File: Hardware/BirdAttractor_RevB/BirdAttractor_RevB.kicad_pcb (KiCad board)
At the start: 2 copper layers, 48.3 x 48.3 mm, 15 parts, among them P1 CONN_01X06, U1 PR_Relay_V23079, U2 DS1305, Y1 Crystal_Small

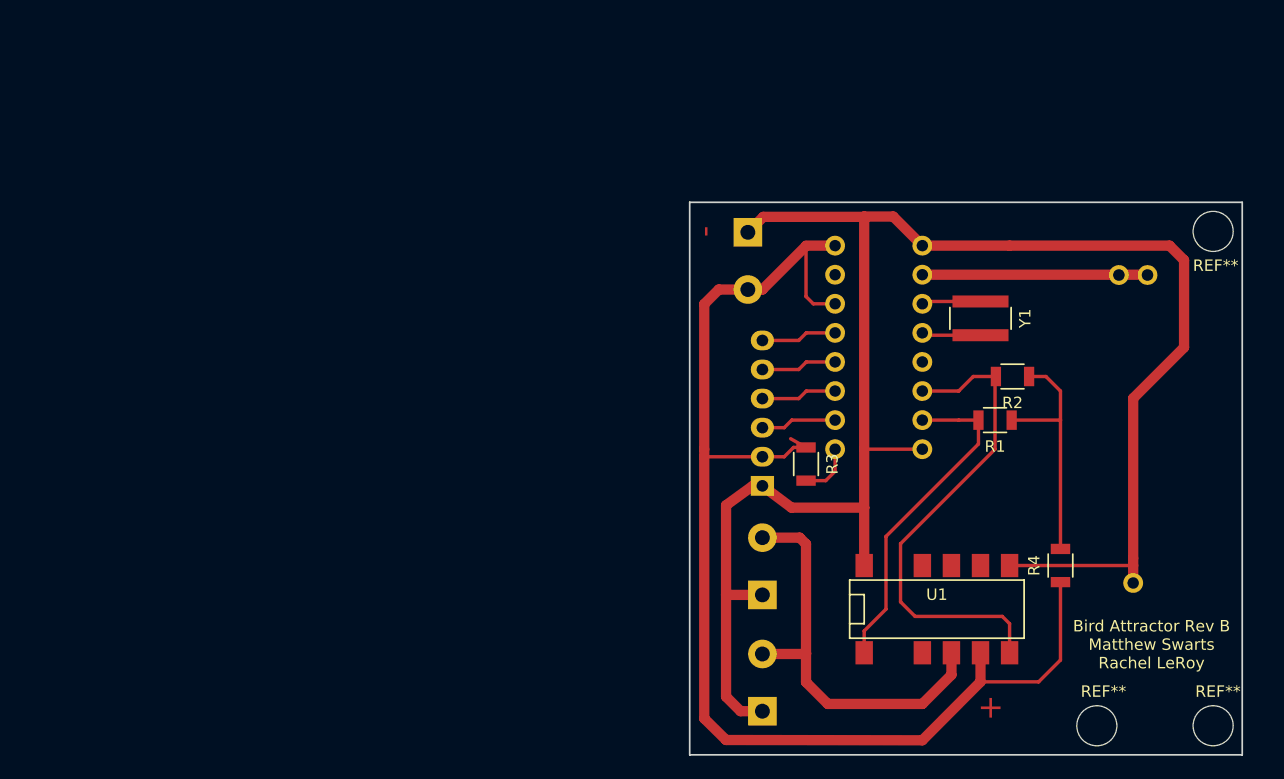
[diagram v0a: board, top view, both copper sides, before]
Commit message: added notes on parts in readme, added new revision to the board with newly selected parts
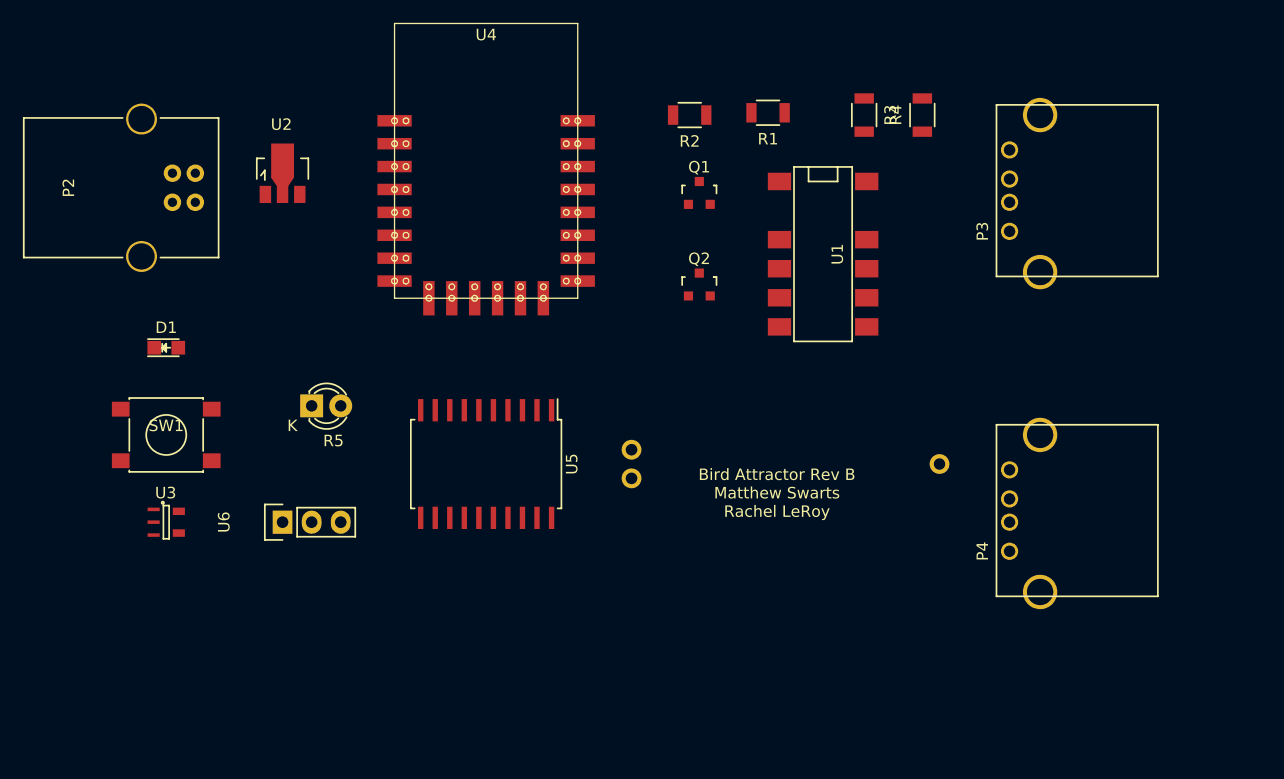
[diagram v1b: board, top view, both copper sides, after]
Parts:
- removed BT2: 5V Battery, Terminal_Blocks:TerminalBlock_Pheonix_MKDS1.5-2pol
- removed P1: CONN_01X06, Socket_Strips:Socket_Strip_Straight_1x06
- removed REF** (x3): 3.2mm_Dia, MyKiCadParts:MountingHole_3-2mm_Dia
- removed SP1, SP2: SPEAKER, Terminal_Blocks:TerminalBlock_Pheonix_MKDS1.5-2pol
- removed Y1: Crystal_Small, Resistors_SMD:R_1218
- added D1: LED, LEDs:LED-0805, F.Cu at (91.4, 96.5)
- added P2: USB_B, Connect:USB_B, F.Cu at (94.0, 83.8)
- added P3: USB_A, Connect:USB_A, F.Cu at (165.1, 86.4)
- added P4: USB_A, Connect:USB_A, F.Cu at (165.1, 114.3)
- added Q1: BSS138, TO_SOT_Packages_SMD:SOT-23, F.Cu at (138.0, 83.0)
- added Q2: BSS138, TO_SOT_Packages_SMD:SOT-23, F.Cu at (138.0, 91.0)
- added R5: Photores, LEDs:LED-3MM, F.Cu at (104.1, 101.6)
- added SW1: SW_PUSH, Buttons_Switches_SMD:SW_SPST_PTS645, F.Cu at (91.4, 104.1)
- added U3: SN74LVC1G14, MyKiCadParts:SOT-23-5-80, F.Cu at (91.4, 111.8)
- added U4: ESP8266-12E, MyKiCadParts:ESP8266-12E-80, F.Cu at (119.4, 76.2)
- added U5: PCF2129AT, MyKiCadParts:SOIC-20_7.5x12.8mm_Pitch1.27mm-80, F.Cu at (119.4, 106.7)
- added U6: VS18388, Pin_Headers:Pin_Header_Straight_1x03, F.Cu at (101.6, 111.8)
- U2: value DS1305 -> AMS1117-3.3; footprint Housings_DIP:DIP-16_W7.62mm -> TO_SOT_Packages_SMD:SOT89-3_Housing; moved to F.Cu
- moved U2 56.2 mm to (101.6, 81.3), turned to 0 degrees
- moved BT1 46.8 mm to (132.1, 106.7), turned to 0 degrees
- moved U1 41.8 mm to (145.0, 82.0), turned to 270 degrees
- moved R4 41.2 mm to (157.5, 76.2)
- moved R2 36.3 mm to (137.2, 76.2)
- moved R1 33.4 mm to (144.0, 76.0)
- moved R3 30.9 mm to (152.4, 76.2)
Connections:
- R3 pad 1: +5V -> 5V_IN
- R3 pad 2: Net-(R3-Pad2) -> (no net)
- R4 pad 1: +5V -> 5V_IN
- U1 pad 10: Net-(U1-Pad10) -> (no net)
- U1 pad 12: GND -> 5V_IN
- U1 pad 3: Net-(U1-Pad3) -> (no net)
- U1 pad 4: LOAD -> 5V_OUT
- U1 pad 5: +5V -> 5V_IN
- U1 pad 7: GND -> 5V_IN
- U1 pad 8: Net-(U1-Pad8) -> (no net)
- U1 pad 9: Net-(U1-Pad9) -> (no net)
- U2 pad 2: Net-(BT1-Pad1) -> V33
- U2 pad 3: Net-(U2-Pad3) -> 5V_IN
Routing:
- net GND: track 153.4 -> 0.00 mm
- net +5V: track 112.1 -> 0.00 mm
- net Net-(R2-Pad2): track 42.9 -> 0.00 mm
- net LOAD: track 36.5 -> 0.00 mm
- net Net-(R1-Pad2): track 29.4 -> 0.00 mm
- net Net-(R1-Pad1): track 21.3 -> 0.00 mm
- net Net-(BT1-Pad1): track 19.7 -> 0.00 mm
- net Net-(P1-Pad6): track 6.62 -> 0.00 mm
- net Net-(P1-Pad4): track 6.62 -> 0.00 mm
- net Net-(P1-Pad5): track 6.62 -> 0.00 mm
- net Net-(P1-Pad3): track 6.62 -> 0.00 mm
- net Net-(U2-Pad4): track 5.16 -> 0.00 mm
- net Net-(U2-Pad3): track 5.16 -> 0.00 mm
- net Net-(R3-Pad2): track 5.06 -> 0.00 mm
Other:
- board outline removed
- board text removed: "+"
- board text removed: "-"

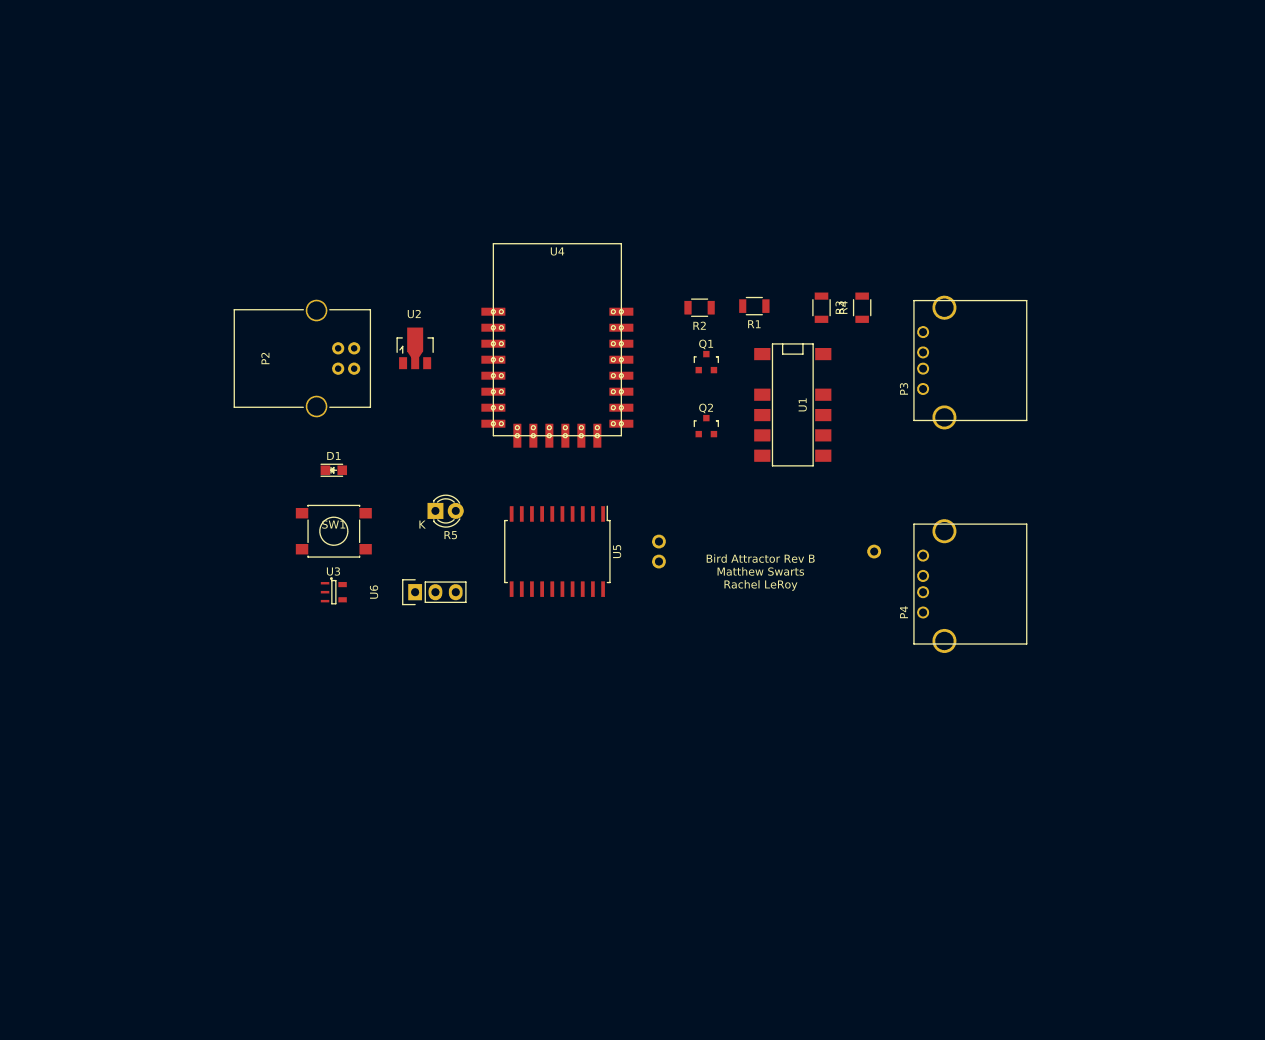
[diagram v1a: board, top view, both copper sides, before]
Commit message: added low pass debounce filter, added connections for different wake up functions, began layout design for in house pcb.
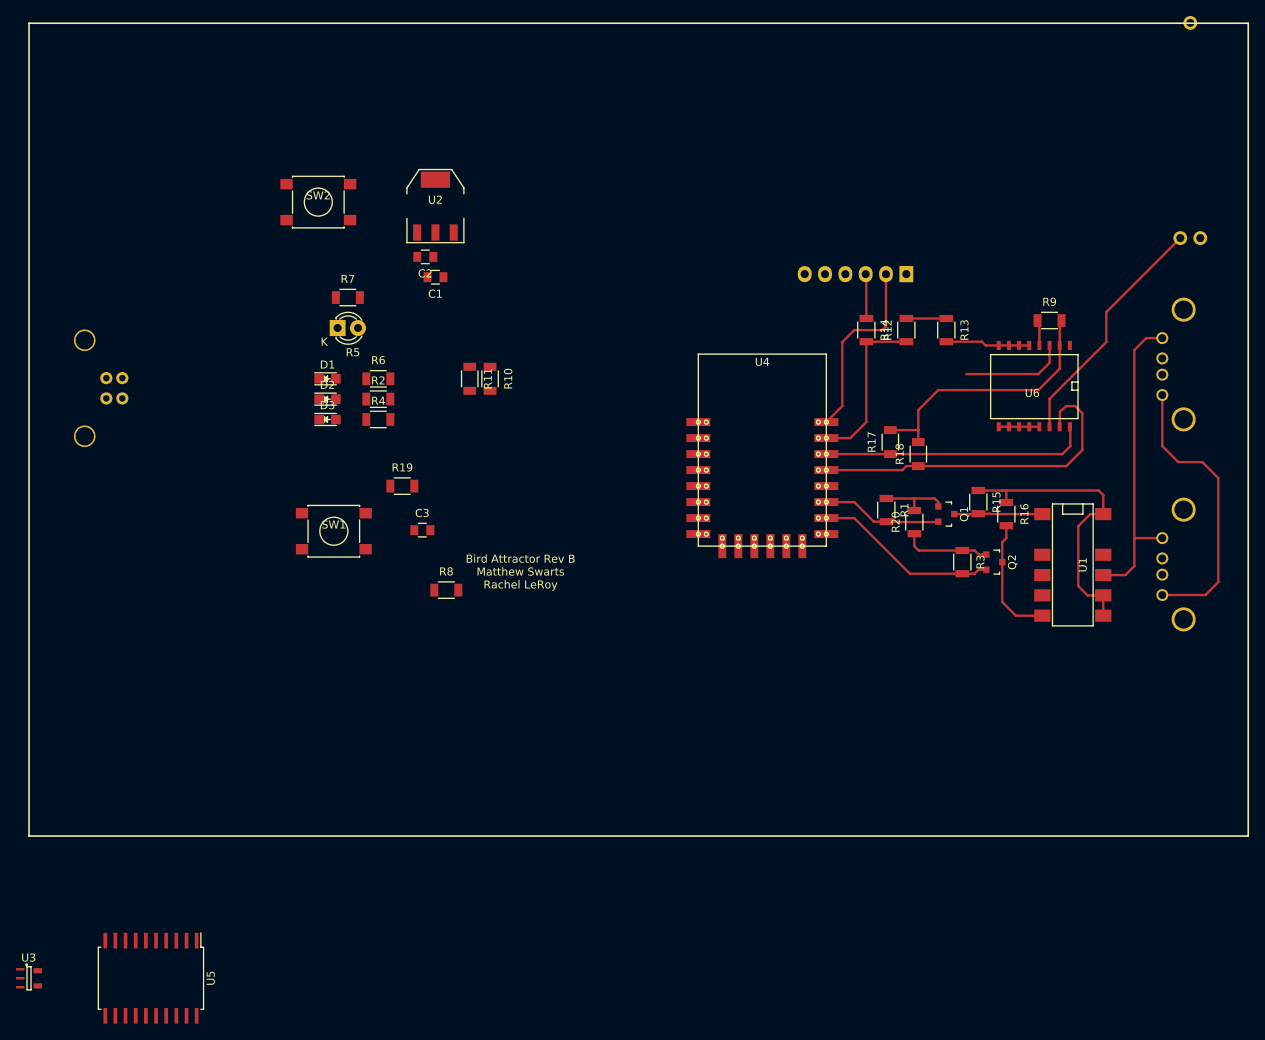
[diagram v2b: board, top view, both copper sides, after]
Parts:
- added C1: 1uF, Capacitors_SMD:C_0805, F.Cu at (104.1, 72.4)
- added C2: 10uF, Capacitors_SMD:C_0805, F.Cu at (102.9, 69.8)
- added C3: 0.1uF, Capacitors_SMD:C_0805, F.Cu at (102.5, 104.0)
- added D2: LED, LEDs:LED-0805, F.Cu at (90.7, 87.6)
- added D3: LED, LEDs:LED-0805, F.Cu at (90.7, 90.2)
- added P1: FTDI, Pin_Headers:Pin_Header_Angled_1x06, B.Cu at (163.0, 72.0)
- added R10: 10K, Capacitors_SMD:C_1206, F.Cu at (111.0, 85.1)
- added R11: 10K, Capacitors_SMD:C_1206, F.Cu at (108.4, 85.1)
- added R12: 10K, Resistors_SMD:R_1206, F.Cu at (163.0, 79.0)
- added R13: 10K, Resistors_SMD:R_1206, F.Cu at (168.0, 79.0)
- added R14: 10K/0, Resistors_SMD:R_1206, F.Cu at (158.0, 79.0)
- added R15: 10K, Resistors_SMD:R_1206, F.Cu at (172.0, 100.5)
- added R16: 10K, Resistors_SMD:R_1206, F.Cu at (175.5, 102.0)
- added R17: 47K, Capacitors_SMD:C_1206, F.Cu at (161.0, 93.0)
- added R18: 47K, Capacitors_SMD:C_1206, F.Cu at (164.5, 94.5)
- added R19: 1K, Capacitors_SMD:C_1206, F.Cu at (100.0, 98.5)
- added R20: 0, Resistors_SMD:R_1206, F.Cu at (164.0, 103.0)
- added R6: 18, Capacitors_SMD:C_1206, F.Cu at (97.0, 85.1)
- added R7: 1K, Capacitors_SMD:C_1206, F.Cu at (93.2, 74.9)
- added R8: 2.7K, Capacitors_SMD:C_1206, F.Cu at (105.5, 111.5)
- added R9: 100K, Capacitors_SMD:C_1206, F.Cu at (180.9, 77.8)
- added SW2: SW_PUSH, Buttons_Switches_SMD:SW_SPST_PTS645, F.Cu at (89.5, 63.0)
- P2, P3, P4: moved to B.Cu
- R1, R3: value 1K -> 10K
- R2: value 1K -> 68; footprint Resistors_SMD:R_1206 -> Capacitors_SMD:C_1206
- R4: value 0 -> 68; footprint Resistors_SMD:R_1206 -> Capacitors_SMD:C_1206
- U2: footprint TO_SOT_Packages_SMD:SOT89-3_Housing -> TO_SOT_Packages_SMD:SOT-223
- U6: value VS18388 -> DS3231; footprint Pin_Headers:Pin_Header_Straight_1x03 -> SMD_Packages:SO-16-W
- moved U6 81.6 mm to (179.0, 86.0), turned to 180 degrees
- moved BT1 77.1 mm to (198.5, 67.5), turned to 90 degrees
- moved U5 73.7 mm to (68.6, 160.0)
- moved R4 62.1 mm to (97.0, 90.2), turned to 0 degrees
- moved U3 61.5 mm to (53.3, 160.0)
- moved R2 41.8 mm to (97.0, 87.6), turned to 0 degrees
- moved U1 40.3 mm to (180.0, 102.0)
- moved Q2 39.8 mm to (174.0, 108.0), turned to 270 degrees
- moved R3 36.3 mm to (170.0, 108.0)
- moved Q1 35.5 mm to (168.0, 102.0), turned to 270 degrees
- moved P4 31.3 mm to (195.0, 105.0), turned to 270 degrees
- moved P3 30.6 mm to (195.0, 80.0), turned to 270 degrees
- moved R1 30.4 mm to (160.5, 101.5), turned to 270 degrees
- moved U4 29.1 mm to (145.0, 90.0)
- moved P2 29.0 mm to (65.0, 85.0)
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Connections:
- BT1 pad 1: Net-(BT1-Pad1) -> VBAT
- D1 pad 1: (no net) -> GND
- D1 pad 2: (no net) -> Net-(D1-Pad2)
- Q1 pad 1: (no net) -> V33
- Q1 pad 2: (no net) -> RELAY_OFF33
- Q1 pad 3: (no net) -> RELAY_OFF
- Q2 pad 1: (no net) -> V33
- Q2 pad 2: (no net) -> RELAY_ON33
- Q2 pad 3: (no net) -> RELAY_ON
- R1 pad 1: Net-(R1-Pad1) -> V33
- R1 pad 2: Net-(R1-Pad2) -> RELAY_OFF33
- R2 pad 1: Net-(R1-Pad1) -> Net-(D2-Pad2)
- R2 pad 2: Net-(R2-Pad2) -> LED_5V_IN
- R3 pad 1: 5V_IN -> V33
- R3 pad 2: (no net) -> RELAY_ON33
- R4 pad 1: 5V_IN -> Net-(D3-Pad2)
- R4 pad 2: Net-(R1-Pad1) -> LED_5V_OUT
- R5 pad 1: (no net) -> V33
- R5 pad 2: (no net) -> ADC
- SW1 pad 2: Net-(SW1-Pad2) -> GND
- U1 pad 1: Net-(R1-Pad2) -> RELAY_OFF
- U1 pad 4: 5V_OUT -> (no net)
- U1 pad 5: 5V_IN -> (no net)
- U1 pad 6: Net-(R2-Pad2) -> RELAY_ON
- U1 pad 8: (no net) -> 5V_IN
- U1 pad 9: (no net) -> 5V_OUT
- U4 pad 1: (no net) -> ALARM_WAKE
- U4 pad 16: (no net) -> RELAY_ON33
- U4 pad 17: (no net) -> RELAY_OFF33
- U4 pad 18: (no net) -> PROGRAM
- U4 pad 19: (no net) -> SDA
- U4 pad 2: (no net) -> ADC
- U4 pad 20: (no net) -> SCL
- U4 pad 21: (no net) -> RX33
- U4 pad 22: (no net) -> TX
- U4 pad 3: (no net) -> CH_PD
- U4 pad 4: (no net) -> DEEP_SLEEP_WAKE
- U4 pad 5: (no net) -> LED_WIFI
- U4 pad 6: (no net) -> LED_5V_IN
- U4 pad 7: (no net) -> LED_5V_OUT
- U6 pad 2: (no net) -> V33
- U6 pad 3: (no net) -> ALARM_WAKE
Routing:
- net V33: track 0.00 -> 53.2 mm
- net GND: track 0.00 -> 51.4 mm
- net SDA: track 0.00 -> 43.0 mm
- net 5V_OUT: track 0.00 -> 39.0 mm
- net 5V_IN: track 0.00 -> 37.1 mm
- net SCL: track 0.00 -> 33.5 mm
- net VBAT: track 0.00 -> 30.4 mm
- net TX: track 0.00 -> 23.6 mm
- net RELAY_ON33: track 0.00 -> 23.1 mm
- net RX33: track 0.00 -> 20.9 mm
- net RELAY_ON: track 0.00 -> 15.5 mm
- net RELAY_OFF33: track 0.00 -> 15.1 mm
- net ALARM_WAKE: track 0.00 -> 13.2 mm
- net RELAY_OFF: track 0.00 -> 11.0 mm
- net RX: track 0.00 -> 5.58 mm
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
